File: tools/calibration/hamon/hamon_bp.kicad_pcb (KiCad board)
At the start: 2 copper layers, 35 x 30 mm, 11 parts, among them SW1 SW_DPST

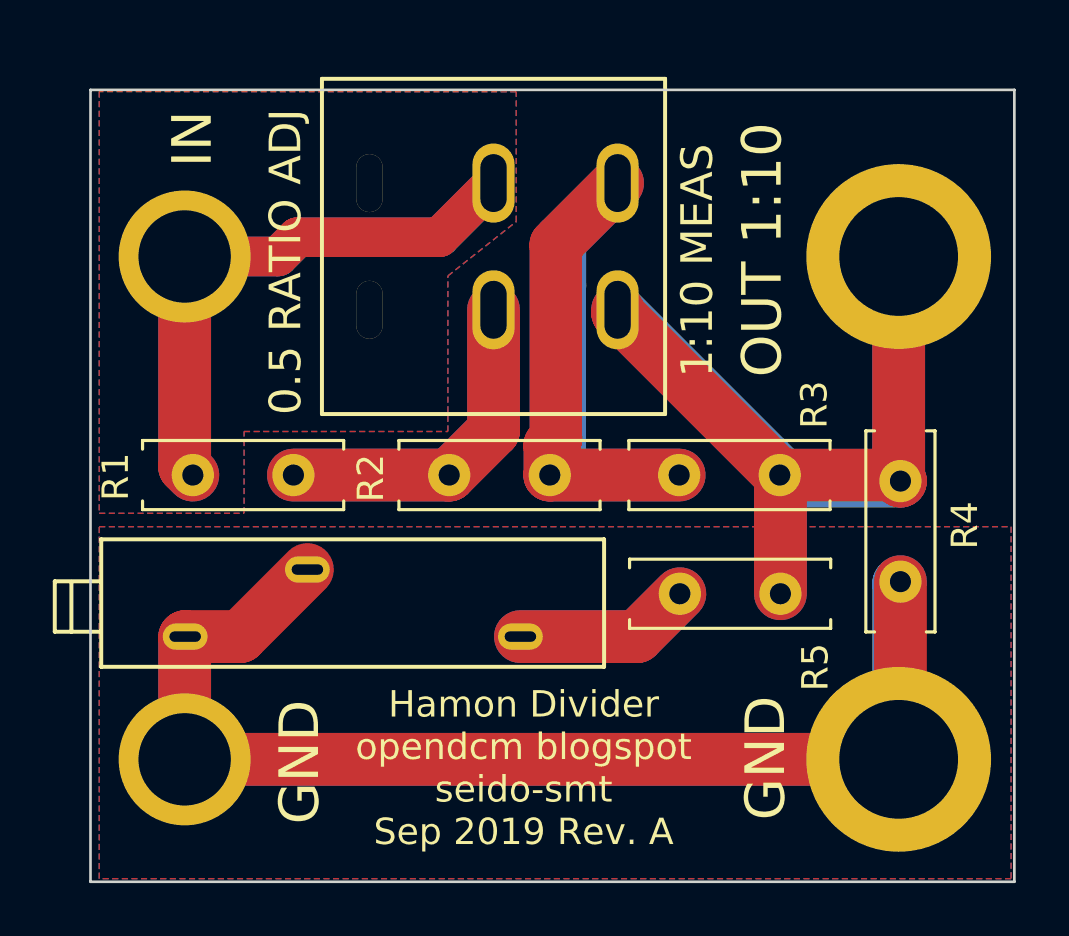
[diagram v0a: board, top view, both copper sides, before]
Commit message: Added second hamon divider PCB with binding posts only. The first variant was with SA404 4mm banana plugs for direct plugin into the voltage reference.
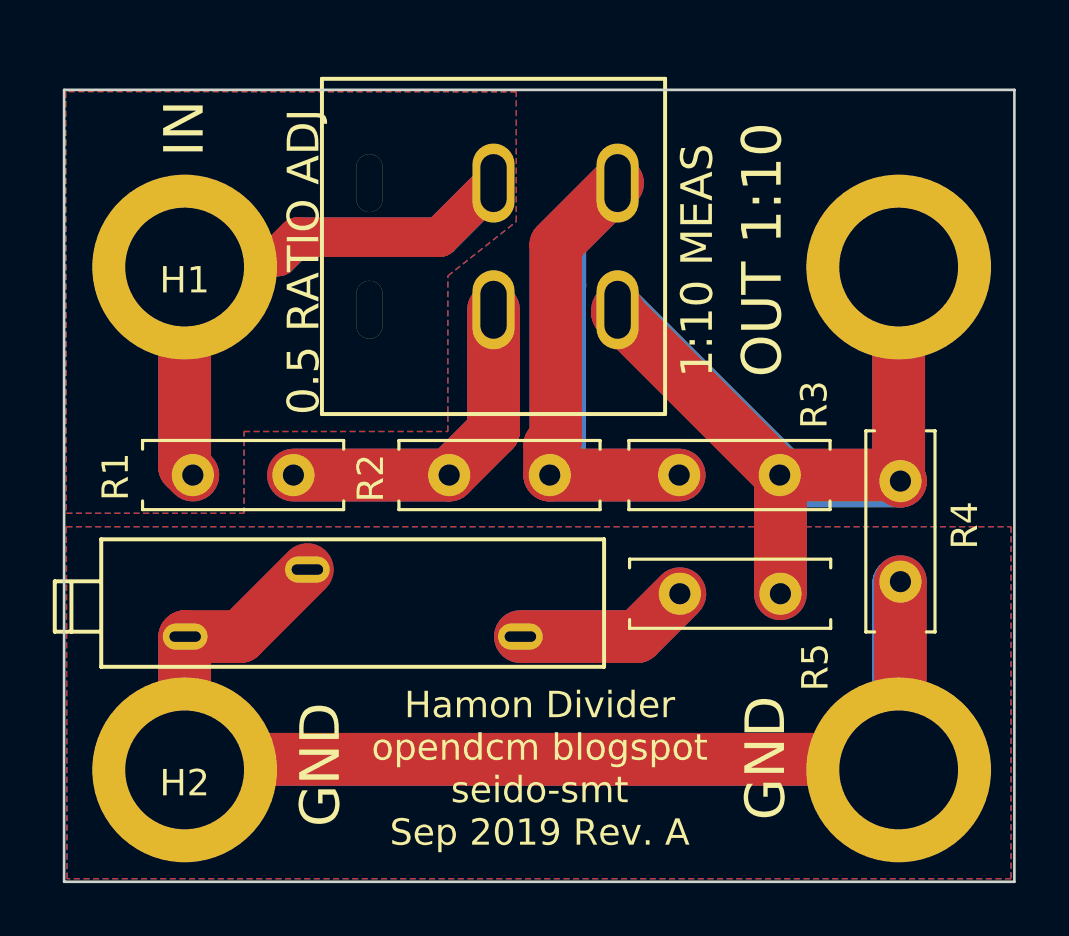
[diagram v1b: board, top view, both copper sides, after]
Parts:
- H1, H2: footprint hamon:SA404 -> hamon:Binding_Post_4mm
- moved H1 0.40 mm to (103.6, 56.7)
- moved H3 0.40 mm to (130.6, 56.7)
- moved H2 0.40 mm to (103.6, 75.8)
- moved H4 0.40 mm to (130.6, 75.8)
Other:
- board size 35 x 30 mm -> 36 x 30 mm
